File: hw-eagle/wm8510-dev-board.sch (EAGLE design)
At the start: 32 parts, among them IC1 WM8510, J1 POWER-CON

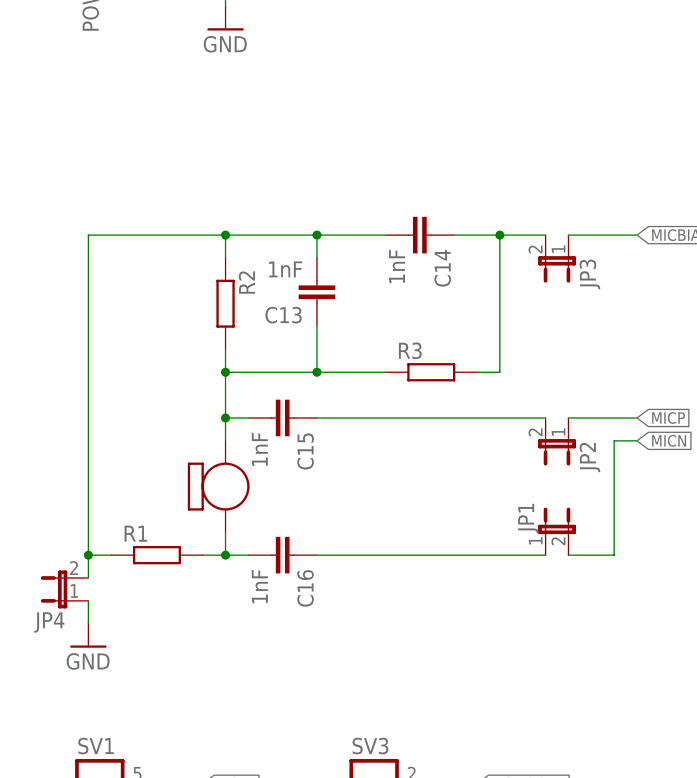
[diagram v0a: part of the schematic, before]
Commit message: Fix the values ​​of resistors and capacitors consisting microphone source .
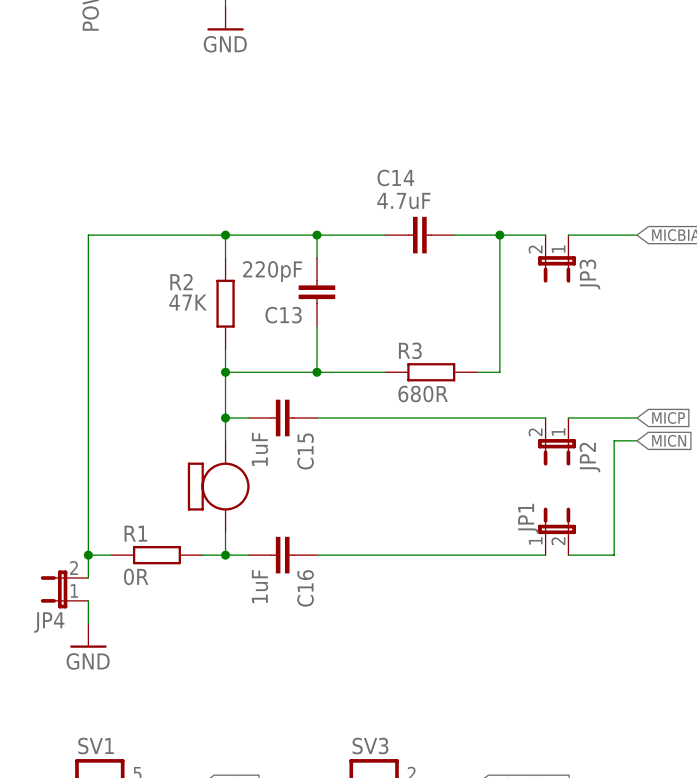
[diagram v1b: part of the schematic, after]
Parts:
- C13: value 1nF -> 220pF
- C14: value 1nF -> 4.7uF
- C15, C16: value 1nF -> 1uF
- R1: value (none) -> 0R
- R2: value (none) -> 47K
- R3: value (none) -> 680R
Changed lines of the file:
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@@
 <part name="JP2" library="jumper" deviceset="JP1E" device=""/>
 <part name="JP3" library="jumper" deviceset="JP1E" device=""/>
-<part name="R1" library="rcl" deviceset="R-EU_" device="M2012"/>
-<part name="R2" library="rcl" deviceset="R-EU_" device="M2012"/>
-<part name="R3" library="rcl" deviceset="R-EU_" device="M2012"/>
-<part name="C13" library="rcl" deviceset="C-EU" device="C1206" value="1nF"/>
-<part name="C14" library="rcl" deviceset="C-EU" device="C1206" value="1nF"/>
-<part name="C15" library="rcl" deviceset="C-EU" device="C1206" value="1nF"/>
-<part name="C16" library="rcl" deviceset="C-EU" device="C1206" value="1nF"/>
+<part name="R1" library="rcl" deviceset="R-EU_" device="M2012" value="0R"/>
+<part name="R2" library="rcl" deviceset="R-EU_" device="M2012" value="47K"/>
+<part name="R3" library="rcl" deviceset="R-EU_" device="M2012" value="680R"/>
+<part name="C13" library="rcl" deviceset="C-EU" device="C1206" value="220pF"/>
+<part name="C14" library="rcl" deviceset="C-EU" device="C1206" value="4.7uF"/>
+<part name="C15" library="rcl" deviceset="C-EU" device="C1206" value="1uF"/>
+<part name="C16" library="rcl" deviceset="C-EU" device="C1206" value="1uF"/>
 <part name="IC1" library="project-specific-library" deviceset="WM8510" device=""/>
 <part name="GND13" library="supply1" deviceset="GND" device=""/>
@@
 <instance part="JP3" gate="A" x="88.9" y="109.22" rot="R180"/>
 <instance part="R1" gate="G$1" x="43.18" y="76.2"/>
-<instance part="R2" gate="G$1" x="50.8" y="104.14" rot="R270"/>
+<instance part="R2" gate="G$1" x="50.8" y="104.14" smashed="yes" rot="R270">
+<attribute name="NAME" x="44.45" y="105.6386" size="1.778" layer="95"/>
+<attribute name="VALUE" x="44.45" y="103.378" size="1.778" layer="96"/>
+</instance>
 <instance part="R3" gate="G$1" x="73.66" y="96.52"/>
-<instance part="C13" gate="G$1" x="60.96" y="104.14" rot="R180"/>
-<instance part="C14" gate="G$1" x="73.66" y="111.76" rot="R270"/>
+<instance part="C13" gate="G$1" x="60.96" y="104.14" smashed="yes" rot="R180">
+<attribute name="NAME" x="59.436" y="103.759" size="1.778" layer="95" rot="R180"/>
+<attribute name="VALUE" x="59.436" y="108.839" size="1.778" layer="96" rot="R180"/>
+</instance>
+<instance part="C14" gate="G$1" x="73.66" y="111.76" smashed="yes" rot="R270">
+<attribute name="NAME" x="67.564" y="117.221" size="1.778" layer="95"/>
+<attribute name="VALUE" x="67.564" y="114.681" size="1.778" layer="96"/>
+</instance>
 <instance part="C15" gate="G$1" x="58.42" y="91.44" rot="R270"/>
 <instance part="C16" gate="G$1" x="58.42" y="76.2" rot="R270"/>

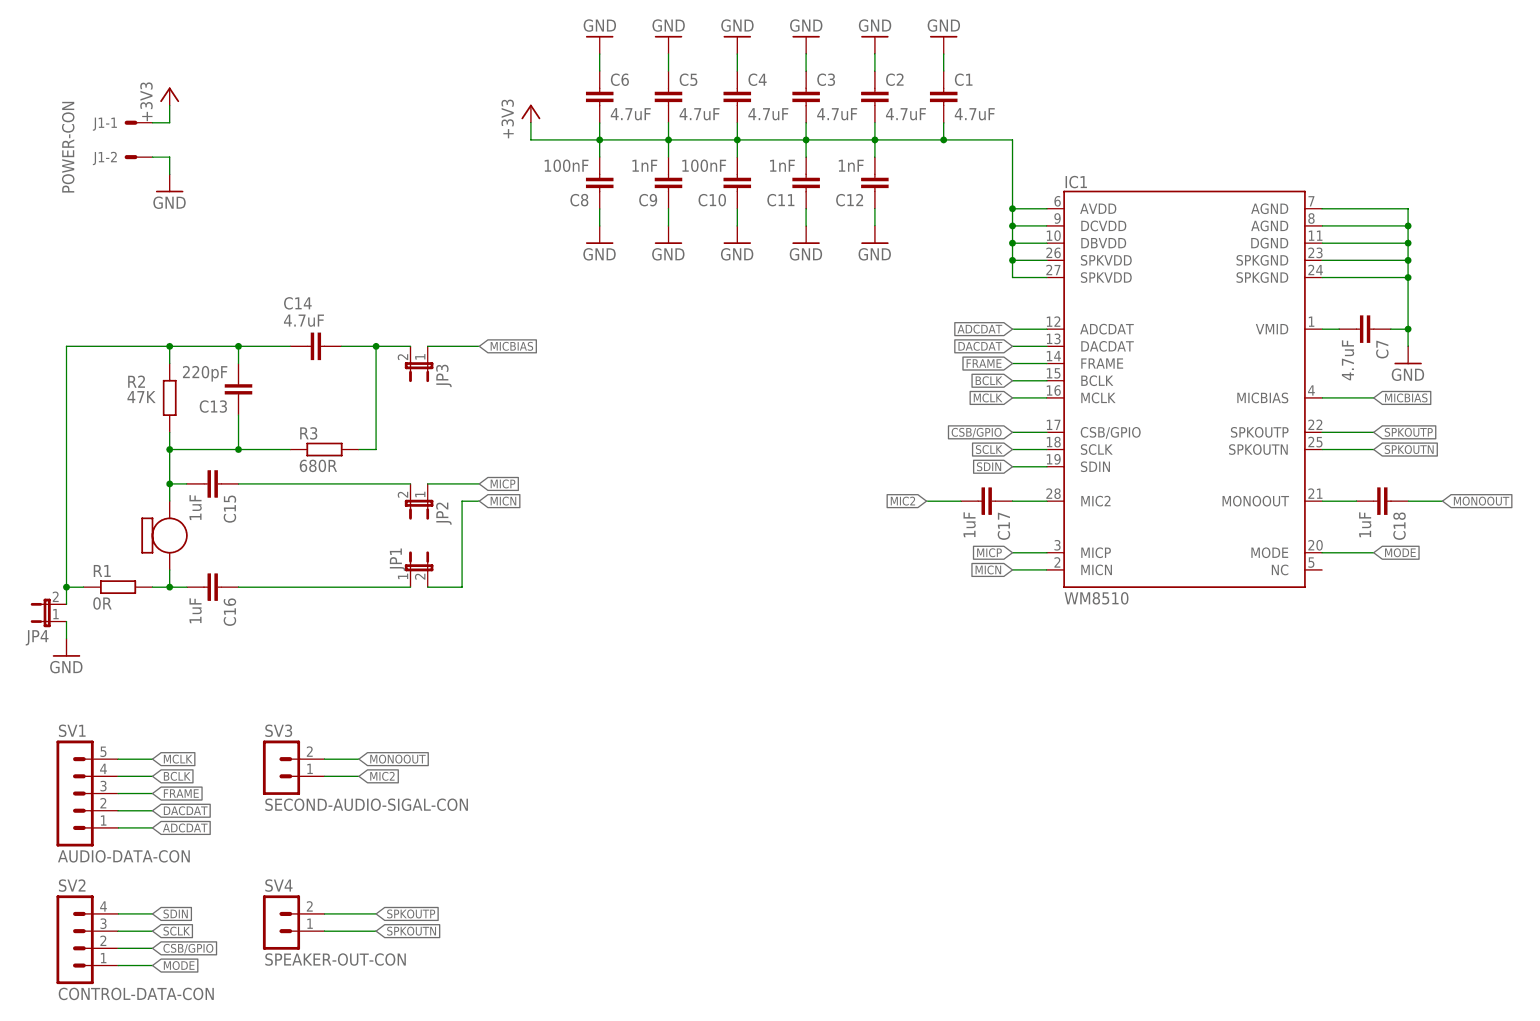
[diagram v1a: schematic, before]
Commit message: I created brd and I routed all routes.
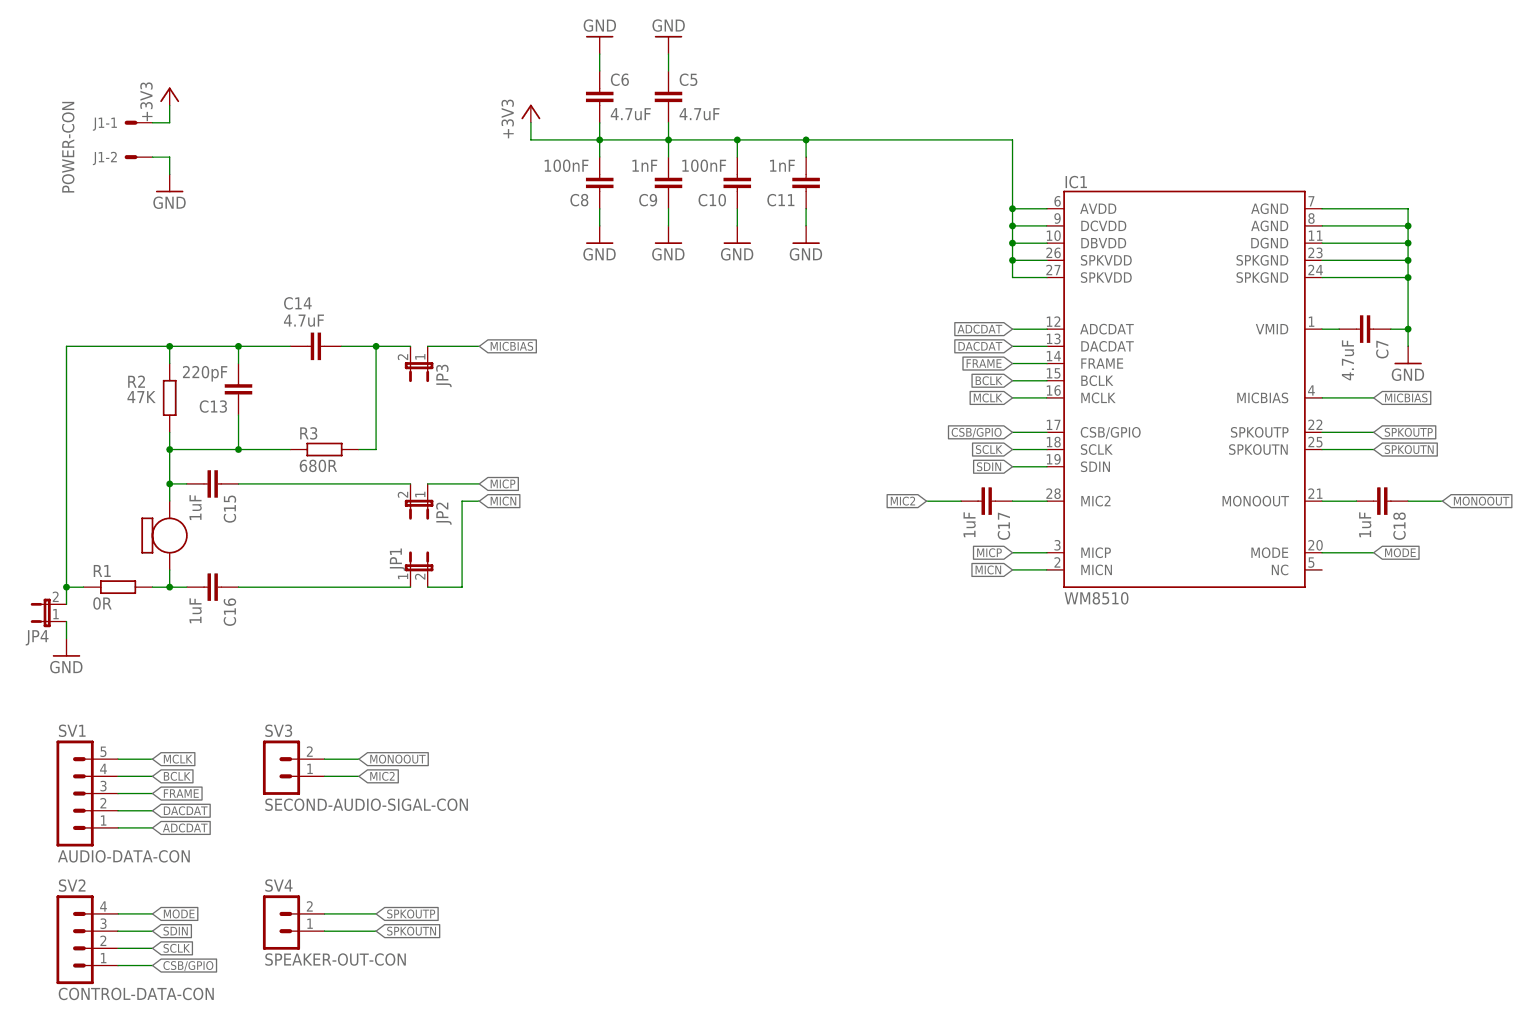
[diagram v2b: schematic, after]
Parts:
- removed C1, C2, C3, C4: 4.7uF, rcl:C-EUC1206
- removed C12: 1nF, rcl:C-EUC1206
- R1, R2, R3: device rcl:R-EU_M2012 -> rcl:R-EU_R1206
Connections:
- removed net AVDD: C1.2, C10.2, C11.2, C12.2, C2.2, C3.2, C4.2, C5.2, C6.2, C8.2, C9.2, IC1.AVDD, IC1.DBVDD, IC1.DCVDD, IC1.SPKVDD@1, IC1.SPKVDD@2
- net +3V3: now also C10.2, C11.2, C5.2, C6.2, C8.2, C9.2, IC1.AVDD, IC1.DBVDD, IC1.DCVDD, IC1.SPKVDD@1, IC1.SPKVDD@2
- net CSB/GPIO: now also SV2.1; no longer SV2.2
- net GND: no longer C1.1, C12.1, C2.1, C3.1, C4.1
- net MODE: now also SV2.4; no longer SV2.1
- net SCLK: now also SV2.2; no longer SV2.3
- net SDIN: now also SV2.3; no longer SV2.4
